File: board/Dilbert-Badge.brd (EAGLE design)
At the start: 105.4 x 52.1 mm, 39 parts, among them IC1 MCP23017SO, J1 IO EXP., J2 FTDI_DEVICE, J3 NEOPIXEL, J5 I2C, SW1 UP, SW2 DOWN, SW3 LEFT, SW4 RIGHT, SW5 A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

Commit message: more layout
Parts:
- moved C1 61.2 mm to (74.9, 59.7), turned to 0 degrees
- moved J2 46.2 mm to (10.2, 53.3)
- moved R6 33.9 mm to (15.9, 41.9), turned to 270 degrees
- moved X1 26.2 mm to (27.9, 43.2), turned to 0 degrees
- moved R3 23.3 mm to (26.7, 40.0), turned to 180 degrees
- moved SW8 20.3 mm to (52.1, 53.3), flipped to the top
- moved SW7 20.3 mm to (41.9, 53.3), flipped to the top
- moved R1 17.9 mm to (41.9, 46.4)
- moved JP5 17.6 mm to (2.54, 45.7)
- moved R5 14.2 mm to (48.3, 45.7)
- moved R2 13.1 mm to (30.5, 43.8), turned to 180 degrees
- moved J5 6.35 mm to (41.9, 7.62), turned to 0 degrees
- moved JP4 5.68 mm to (29.2, 24.1), turned to 180 degrees
- moved R7 3.18 mm to (62.2, 27.3)
- moved R4 1.80 mm to (63.5, 17.8), turned to 0 degrees
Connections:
- removed net VDD: LED2.1-VDD, LED3.1-VDD, LED4.1-VDD, LED5.1-VDD, LED6.1-VDD, LED7.1-VDD
- net 3V3: now also LED2.1-VDD, LED3.1-VDD, LED4.1-VDD, LED5.1-VDD, LED6.1-VDD, LED7.1-VDD
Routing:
- net 3V3: track 31.6 -> 213.5 mm, vias 0 -> 4
- net NEOPIXEL: track 0.00 -> 121.2 mm, vias 0 -> 4
- net TFT_DC: track 0.00 -> 52.2 mm, vias 0 -> 1
- net UART_TX: track 4.17 -> 54.7 mm, vias 0 -> 2
- net SDA: track 13.3 -> 56.6 mm, vias 0 -> 1
- net SCL: track 15.6 -> 56.3 mm, vias 0 -> 1
- net TFT_CS: track 106.2 -> 72.2 mm
- net TFT_BL: track 58.4 -> 32.5 mm, vias 1 -> 0
- net RESET: track 36.0 -> 14.8 mm
- net MCP_IO_INT: track 24.1 -> 41.4 mm, vias 1 -> 3
- net SD_CS: track 10.6 -> 22.0 mm
- net MCP_IO_A0: track 0.00 -> 9.12 mm, vias 0 -> 1
- net MCP_IO_A2: track 0.00 -> 7.92 mm, vias 0 -> 1
- net SCK: track 79.0 -> 71.4 mm, vias 2 -> 0
- net ESP_CH_PD: track 13.3 -> 5.70 mm
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
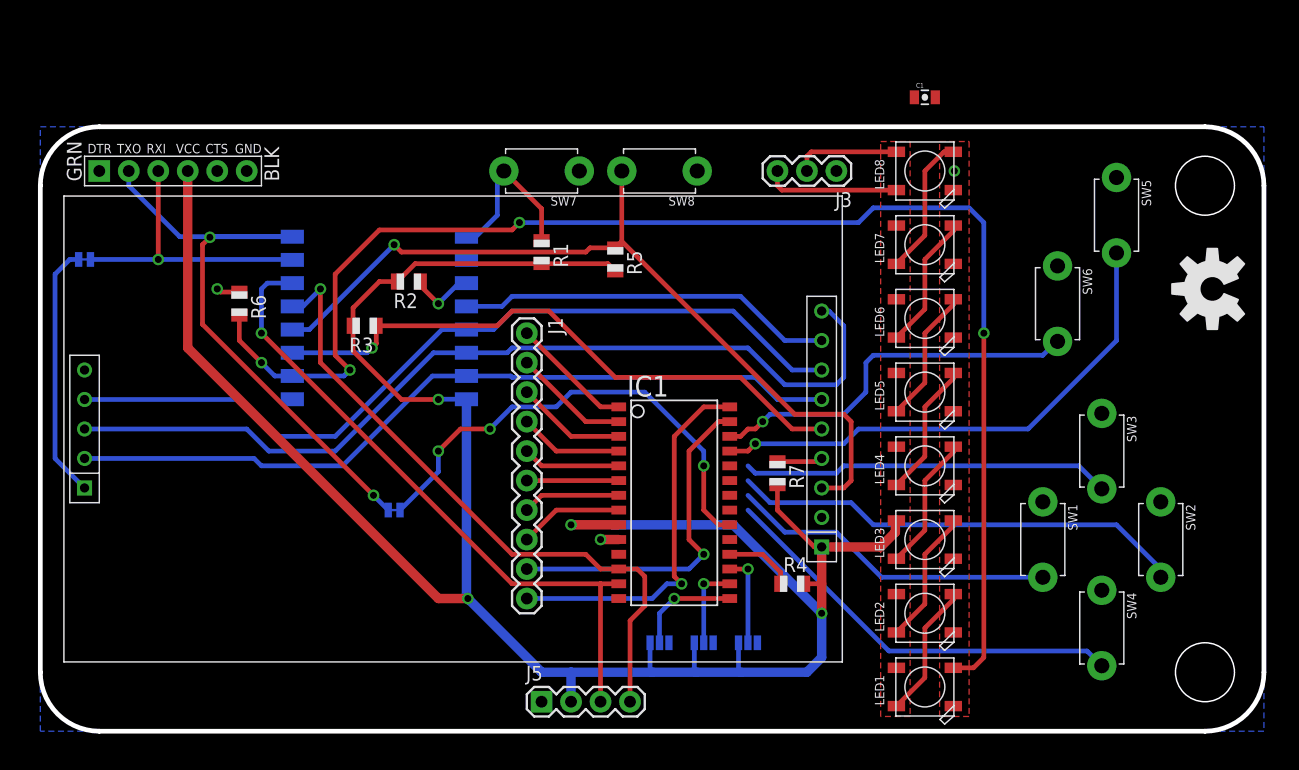
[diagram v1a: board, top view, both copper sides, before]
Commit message: correct switches, more layout
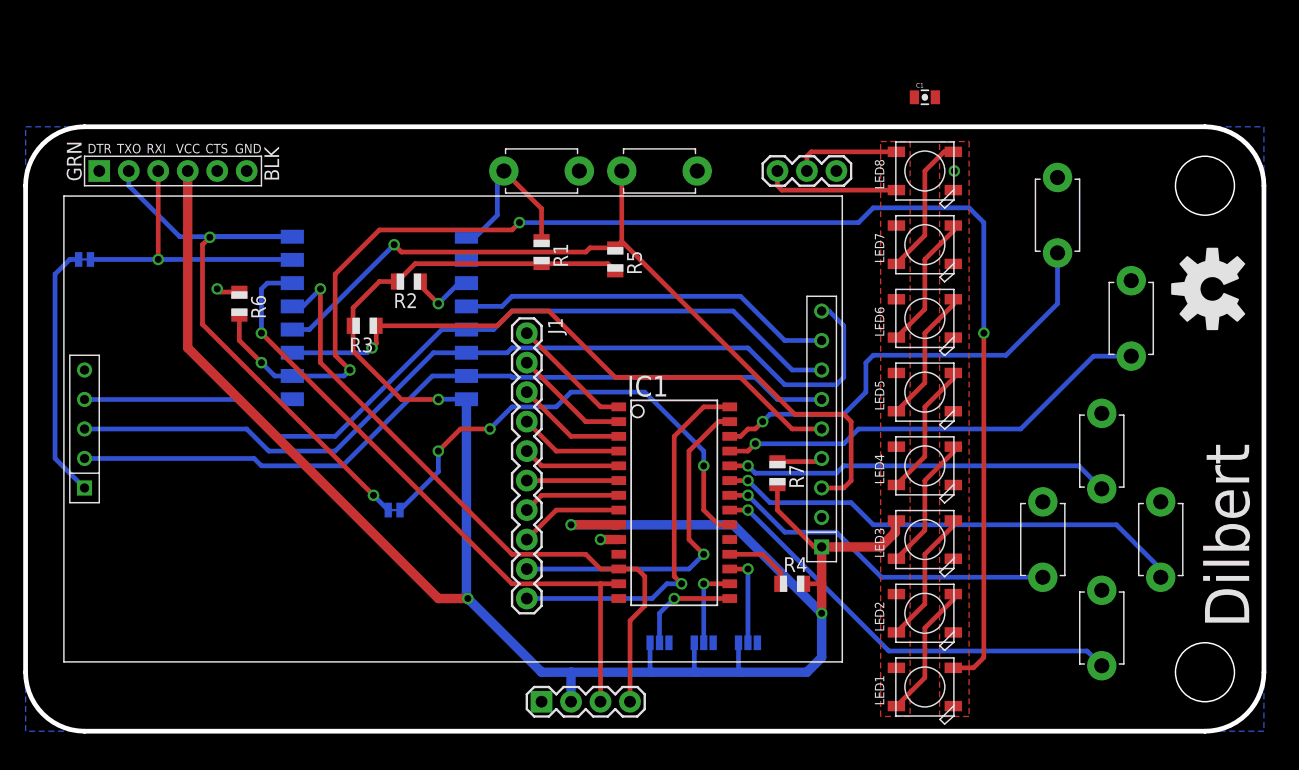
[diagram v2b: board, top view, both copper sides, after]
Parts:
- moved SW5 8.98 mm to (92.7, 40.6)
- moved SW6 7.62 mm to (86.4, 49.5)
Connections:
- net BTN_D: now also IC1.23; no longer IC1.22
- net BTN_L: now also IC1.24; no longer IC1.23
- net BTN_R: now also IC1.21; no longer IC1.24
- net BTN_U: now also IC1.22; no longer IC1.21
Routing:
- net BTN_A: track 44.8 -> 38.0 mm
- net BTN_B: track 33.1 -> 38.8 mm
- net BTN_U: track 28.3 -> 29.9 mm, vias 0 -> 1
- net BTN_R: track 36.0 -> 37.6 mm, vias 0 -> 1
- net BTN_L: track 31.8 -> 33.4 mm, vias 0 -> 1
- net BTN_D: track 39.4 -> 41.0 mm, vias 0 -> 1
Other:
- board size 105.4 x 52.1 mm -> 106.7 x 52.1 mm
- board text added: "Dilbert"

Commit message: more layout
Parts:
- moved C1 71.2 mm to (6.35, 40.6), turned to 180 degrees
- moved JP4 9.09 mm to (37.5, 27.9), turned to 90 degrees
- moved R3 2.54 mm to (29.2, 40.0)
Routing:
- net MCP_IO_INT: track 41.4 -> 32.3 mm, vias 3 -> 1
- net 3V3: track 213.5 -> 208.6 mm
- net UART_TX: track 54.7 -> 58.0 mm
- net NEOPIXEL: track 121.2 -> 121.9 mm
- net TFT_DC: track 52.2 -> 52.8 mm
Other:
- board text added: "2016"
- board text added: "3V3"
- board text added: "DATA"
- board text added: "GND"
- board text added: "SCL"
- board text added: "SDA"

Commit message: ERC/DRU checks
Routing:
- net MOSI: track 67.8 -> 69.9 mm
- net MISO: track 78.3 -> 79.4 mm
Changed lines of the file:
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@@
 </class>
 </classes>
-<designrules name="default">
-<description language="de">&lt;b&gt;EAGLE Design Rules&lt;/b&gt;
-&lt;p&gt;
-Die Standard-Design-Rules sind so gewählt, dass sie für
-die meisten Anwendungen passen. Sollte ihre Platine
-besondere Anforderungen haben, treffen Sie die erforderlichen
-Einstellungen hier und speichern die Design Rules unter
-einem neuen Namen ab.</description>
-<description language="en">&lt;b&gt;EAGLE Design Rules&lt;/b&gt;
-&lt;p&gt;
-The default Design Rules have been set to cover
-a wide range of applications. Your particular design
-may have different requirements, so please make the
-necessary adjustments and save your customized
-design rules under a new name.</description>
+<designrules name="dirt_cheap_dirty_boards.v1">
+<description language="en">&lt;b&gt;Dirty Cheap Dirty Board Design Rules&lt;/b&gt;
+&lt;br&gt;
+&lt;br&gt;Min width/Spacing: 5/5mil
+&lt;br&gt;Min diameter of finished hole 12mil</description>
 <param name="layerSetup" value="(1*16)"/>
-<param name="mtCopper" value="0.035mm 0.035mm 0.035mm 0.035mm 0.035mm 0.035mm 0.035mm 0.035mm 0.035mm 0.035mm 0.035mm 0.035mm 0.035mm 0.035mm 0.035mm 0.035mm"/>
-<param name="mtIsolate" value="1.5mm 0.15mm 0.2mm 0.15mm 0.2mm 0.15mm 0.2mm 0.15mm 0.2mm 0.15mm 0.2mm 0.15mm 0.2mm 0.15mm 0.2mm"/>
-<param name="mdWireWire" value="8mil"/>
-<param name="mdWirePad" value="8mil"/>
-<param name="mdWireVia" value="8mil"/>
-<param name="mdPadPad" value="8mil"/>
-<param name="mdPadVia" value="8mil"/>
-<param name="mdViaVia" value="8mil"/>
-<param name="mdSmdPad" value="8mil"/>
-<param name="mdSmdVia" value="8mil"/>
-<param name="mdSmdSmd" value="8mil"/>
+<param name="mtCopper" value="0.035mm 0.0175mm 0.035mm 0.035mm 0.035mm 0.035mm 0.035mm 0.035mm 0.035mm 0.035mm 0.035mm 0.035mm 0.035mm 0.035mm 0.0175mm 0.035mm"/>
+<param name="mtIsolate" value="1.5mm 1.1mm 0.2mm 0.15mm 0.2mm 0.15mm 0.2mm 0.15mm 0.2mm 0.15mm 0.2mm 0.15mm 0.2mm 0.15mm 0.2mm"/>
+<param name="mdWireWire" value="5mil"/>
+<param name="mdWirePad" value="5mil"/>
+<param name="mdWireVia" value="5mil"/>
+<param name="mdPadPad" value="5mil"/>
+<param name="mdPadVia" value="5mil"/>
+<param name="mdViaVia" value="5mil"/>
+<param name="mdSmdPad" value="0mil"/>
+<param name="mdSmdVia" value="0mil"/>
+<param name="mdSmdSmd" value="0mil"/>
 <param name="mdViaViaSameLayer" value="8mil"/>
 <param name="mnLayersViaInSmd" value="2"/>
-<param name="mdCopperDimension" value="40mil"/>
-<param name="mdDrill" value="8mil"/>
+<param name="mdCopperDimension" value="10mil"/>
+<param name="mdDrill" value="10mil"/>
 <param name="mdSmdStop" value="0mil"/>
-<param name="msWidth" value="10mil"/>
-<param name="msDrill" value="24mil"/>
-<param name="msMicroVia" value="9.99mm"/>
+<param name="msWidth" value="5mil"/>
+<param name="msDrill" value="12mil"/>
+<param name="msMicroVia" value="12mil"/>
 <param name="msBlindViaRatio" value="0.5"/>
 <param name="rvPadTop" value="0.25"/>
@@
 <param name="rlMinPadBottom" value="10mil"/>
 <param name="rlMaxPadBottom" value="20mil"/>
-<param name="rlMinViaOuter" value="8mil"/>
+<param name="rlMinViaOuter" value="6mil"/>
 <param name="rlMaxViaOuter" value="20mil"/>
-<param name="rlMinViaInner" value="8mil"/>
+<param name="rlMinViaInner" value="6mil"/>
 <param name="rlMaxViaInner" value="20mil"/>
 <param name="rlMinMicroViaOuter" value="4mil"/>
@@
 <param name="psTop" value="-1"/>
 <param name="psBottom" value="-1"/>
-<param name="psFirst" value="-1"/>
+<param name="psFirst" value="0"/>
 <param name="psElongationLong" value="100"/>
 <param name="psElongationOffset" value="100"/>
 <param name="mvStopFrame" value="1"/>
 <param name="mvCreamFrame" value="0"/>
-<param name="mlMinStopFrame" value="4mil"/>
-<param name="mlMaxStopFrame" value="4mil"/>
+<param name="mlMinStopFrame" value="2mil"/>
+<param name="mlMaxStopFrame" value="2mil"/>
 <param name="mlMinCreamFrame" value="0mil"/>
 <param name="mlMaxCreamFrame" value="0mil"/>
-<param name="mlViaStopLimit" value="0mil"/>
+<param name="mlViaStopLimit" value="25mil"/>
 <param name="srRoundness" value="0"/>
 <param name="srMinRoundness" value="0mil"/>
@@
 <param name="checkAngle" value="0"/>
 <param name="checkFont" value="1"/>
-<param name="checkRestrict" value="1"/>
+<param name="checkRestrict" value="0"/>
 <param name="useDiameter" value="13"/>
 <param name="maxErrors" value="50"/>
@@
 <contactref element="U$1" pad="MOSI"/>
 <contactref element="U$1" pad="SD_MOSI"/>
-<wire x1="2.54" y1="28.575" x2="17.145" y2="28.575" width="0.4064" layer="16"/>
-<wire x1="17.145" y1="28.575" x2="17.78" y2="27.94" width="0.4064" layer="16"/>
 <wire x1="17.78" y1="27.94" x2="24.765" y2="27.94" width="0.4064" layer="16"/>
 <wire x1="24.765" y1="27.94" x2="32.505" y2="35.68" width="0.4064" layer="16"/>
@@
 <wire x1="60.325" y1="35.56" x2="62.23" y2="33.655" width="0.4064" layer="16"/>
 <wire x1="62.23" y1="33.655" x2="66.04" y2="33.655" width="0.4064" layer="16"/>
+<wire x1="17.78" y1="27.94" x2="14.605" y2="31.115" width="0.4064" layer="16"/>
+<wire x1="14.605" y1="31.115" x2="5.08" y2="31.115" width="0.4064" layer="16"/>
+<wire x1="5.08" y1="31.115" x2="2.54" y2="28.575" width="0.4064" layer="16"/>
 </signal>
 <signal name="MISO">
@@
 <wire x1="32.6" y1="37.68" x2="24.13" y2="29.21" width="0.4064" layer="16"/>
 <wire x1="24.13" y1="29.21" x2="18.415" y2="29.21" width="0.4064" layer="16"/>
-<wire x1="18.415" y1="29.21" x2="16.51" y2="31.115" width="0.4064" layer="16"/>
-<wire x1="16.51" y1="31.115" x2="2.54" y2="31.115" width="0.4064" layer="16"/>
+<wire x1="18.415" y1="29.21" x2="15.24" y2="32.385" width="0.4064" layer="16"/>
+<wire x1="15.24" y1="32.385" x2="3.81" y2="32.385" width="0.4064" layer="16"/>
+<wire x1="3.81" y1="32.385" x2="2.54" y2="31.115" width="0.4064" layer="16"/>
 </signal>
 <signal name="3V3" class="1">
